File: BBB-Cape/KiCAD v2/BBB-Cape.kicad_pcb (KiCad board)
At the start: 2 copper layers, 54.6 x 86.4 mm, 85 parts, among them J1 MOUNTING_HOLE, J10 Conn_01x02, J11 RJ45-TRANSFO, J12 DB9_Female, J13 SPI1, J14 I2C2, J15 UART5, J16 5V PWR, J2 MOUNTING_HOLE, J3 MOUNTING_HOLE, J4 MOUNTING_HOLE, J9 01x06_Stackable Header, P8 02x23_Stackable Header, P9 02x23_Stackable Header, SW1 W5500_RST, SW2 SYS_RST, SW3 Power, U1 LM25576MH, U2 WIZnet W5500, U3 MAX13433EETD, Y1 25MHz

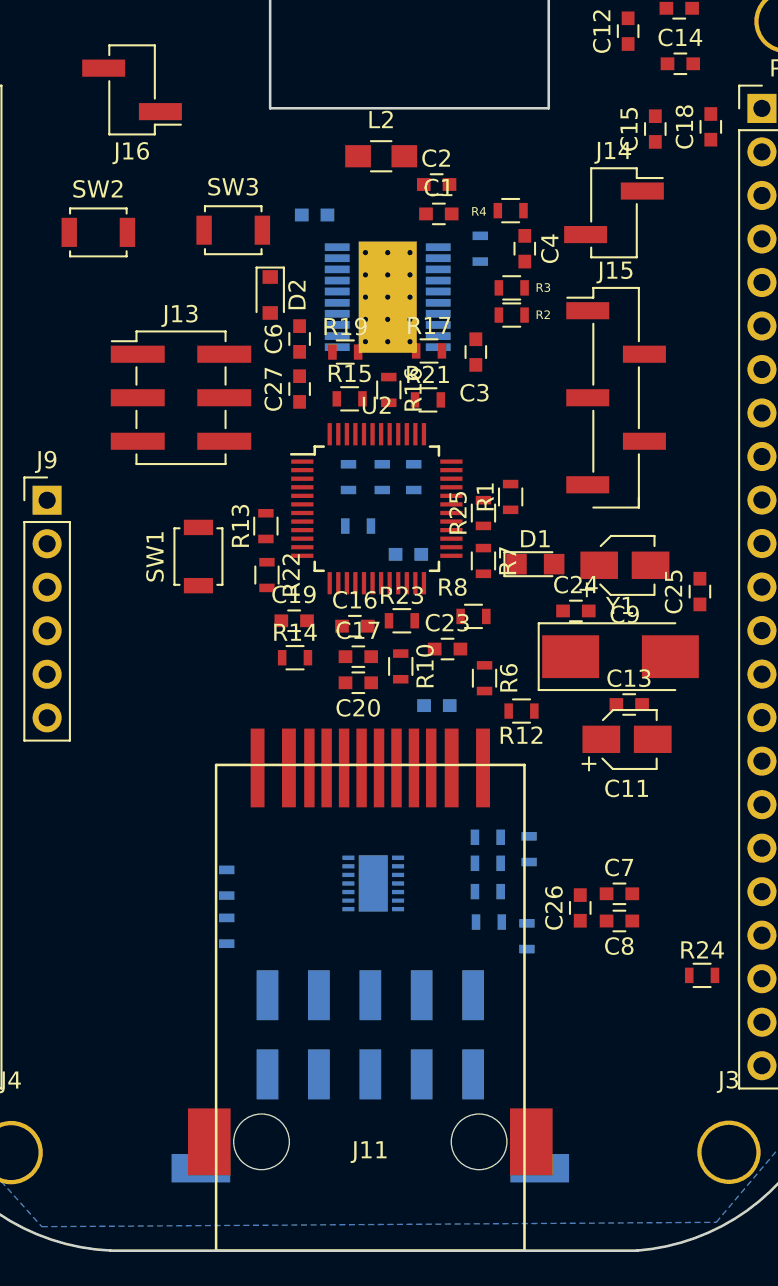
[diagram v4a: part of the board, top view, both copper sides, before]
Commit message: Connector Position Changes
Moved around the ethernet and RS485 connectors so they will not interfere with the BBB.
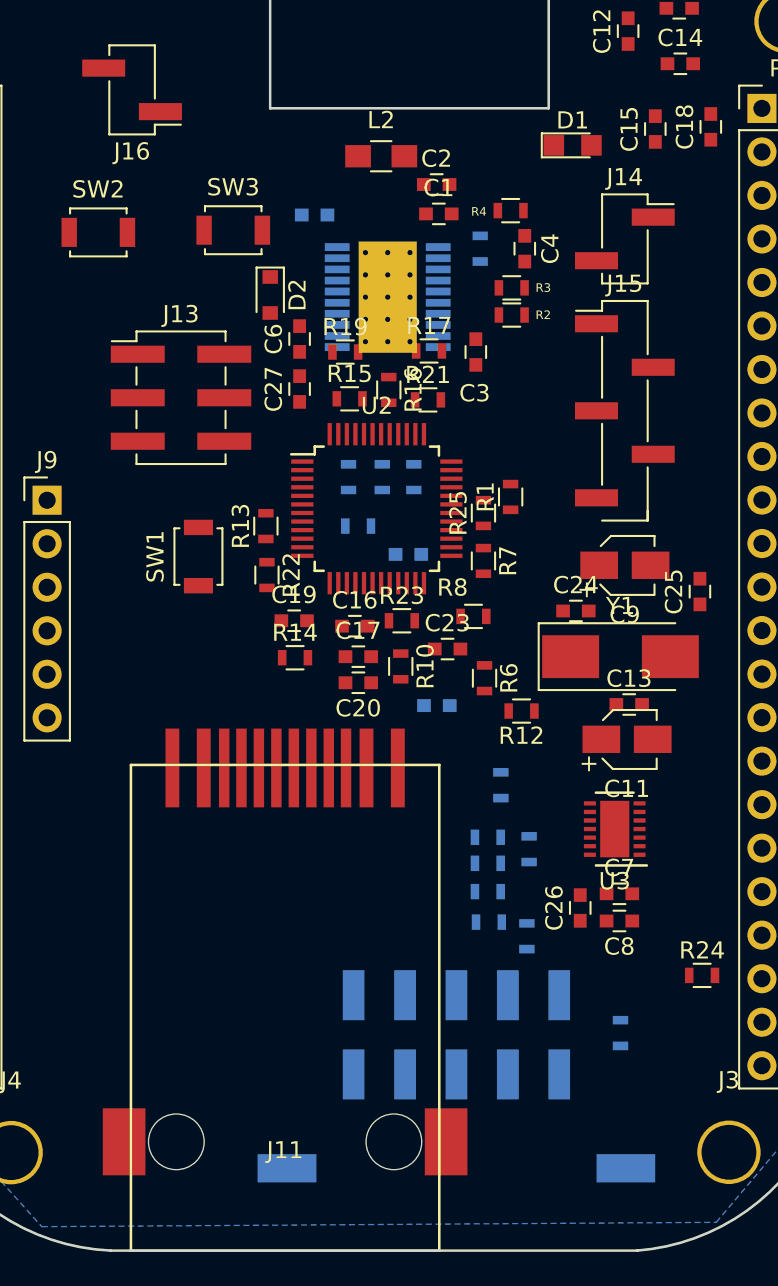
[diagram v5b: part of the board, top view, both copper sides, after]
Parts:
- U3: moved to F.Cu
- moved R32 24.6 mm to (152.6, 121.2)
- moved D1 24.5 mm to (149.8, 69.4)
- moved R33 18.1 mm to (145.6, 106.7)
- moved U3 14.5 mm to (152.2, 109.3)
- moved J12 5.03 mm to (143.0, 121.3)
- moved J11 4.97 mm to (133.0, 127.5)
- moved J14 1.65 mm to (152.8, 74.8)
- moved J15 0.92 mm to (152.8, 84.9)
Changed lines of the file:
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@@
   (general
     (links 206)
-    (no_connects 188)
-    (area 104.279275 45.8891 171.666326 168.8085)
+    (no_connects 187)
+    (area 110.592799 47.461099 165.352801 133.971101)
     (thickness 1.6)
     (drawings 12)
@@
   )
   (setup
-    (last_trace_width 0.254)
+    (last_trace_width 0.4064)
     (user_trace_width 0.254)
     (user_trace_width 0.3048)
@@
   )
   (module Connectors_Molex:Molex_MicroFit_3.0-43045-1010_10x3.00mm_Angled (layer B.Cu)
-    (at 137.9728 121.2991)
+    (at 143 121.2991)
     (descr "Molex Micro-Fit 3.0 connector, PN:43045-1010, top entry type, SMDhttp://www.molex.com/pdm_docs/sd/430450210_sd.pdf")
     (tags "conn molex micro fit 3.0")
@@
   )
   (module RJ45:RJ45_Surface_Mount (layer F.Cu)
-    (at 137.9728 127.5461)
+    (at 133 127.5461)
     (fp_text reference J11 (at 0 0.5) (layer F.SilkS)
       (effects (font (size 1 1) (thickness 0.15)))
@@
   )
   (module LEDs:LED_0805 (layer F.Cu)
-    (at 147.6043 93.8276)
+    (at 149.7838 69.3801)
     (descr "LED 0805 smd package")
     (tags "LED led 0805 SMD smd SMT smt smdled SMDLED smtled SMTLED")
@@
   )
   (module Resistors_SMD:R_0603 (layer B.Cu)
-    (at 129.5908 112.4211 90)
+    (at 152.5778 121.1961 90)
     (descr "Resistor SMD 0603, reflow soldering, Vishay (see dcrcw.pdf)")
     (tags "resistor 0603")
@@
   )
   (module Resistors_SMD:R_0603 (layer B.Cu)
-    (at 129.5908 115.2271 270)
+    (at 145.5928 106.7301 270)
     (descr "Resistor SMD 0603, reflow soldering, Vishay (see dcrcw.pdf)")
     (tags "resistor 0603")
@@
     )
   )
-  (module Housings_DFN_QFN:DFN-14-1EP_3x4mm_Pitch0.5mm (layer B.Cu)
-    (at 138.1438 112.4646 180)
+  (module Housings_DFN_QFN:DFN-14-1EP_3x4mm_Pitch0.5mm (layer F.Cu)
+    (at 152.2408 109.2896 180)
     (descr "DE Package; 14-Lead Plastic DFN (4mm x 3mm) (see Linear Technology DFN_14_05-08-1708.pdf)")
     (tags "DFN 0.5")
     (attr smd)
-    (fp_text reference U3 (at 0 3.05 180) (layer B.SilkS)
-      (effects (font (size 1 1) (thickness 0.15)) (justify mirror))
+    (fp_text reference U3 (at 0 -3.05 180) (layer F.SilkS)
+      (effects (font (size 1 1) (thickness 0.15)))
     )
-    (fp_text value MAX13433EETD (at 0 -3.05 180) (layer B.Fab)
-      (effects (font (size 1 1) (thickness 0.15)) (justify mirror))
+    (fp_text value MAX13433EETD (at 0 3.05 180) (layer F.Fab)
+      (effects (font (size 1 1) (thickness 0.15)))
     )
-    (fp_line (start -0.5 2) (end 1.5 2) (layer B.Fab) (width 0.15))
-    (fp_line (start 1.5 2) (end 1.5 -2) (layer B.Fab) (width 0.15))
-    (fp_line (start 1.5 -2) (end -1.5 -2) (layer B.Fab) (width 0.15))
-    (fp_line (start -1.5 -2) (end -1.5 1) (layer B.Fab) (width 0.15))
-    (fp_line (start -1.5 1) (end -0.5 2) (layer B.Fab) (width 0.15))
-    (fp_line (start -2.05 2.3) (end -2.05 -2.3) (layer B.CrtYd) (width 0.05))
-    (fp_line (start 2.05 2.3) (end 2.05 -2.3) (layer B.CrtYd) (width 0.05))
-    (fp_line (start -2.05 2.3) (end 2.05 2.3) (layer B.CrtYd) (width 0.05))
-    (fp_line (start -2.05 -2.3) (end 2.05 -2.3) (layer B.CrtYd) (width 0.05))
-    (fp_line (start -1.1 -2.125) (end 1.1 -2.125) (layer B.SilkS) (width 0.15))
-    (fp_line (start -1.875 2.125) (end 1.1 2.125) (layer B.SilkS) (width 0.15))
-    (pad 1 smd rect (at -1.45 1.5 180) (size 0.7 0.25) (layers B.Cu B.Paste B.Mask)
+    (fp_line (start -0.5 -2) (end 1.5 -2) (layer F.Fab) (width 0.15))
+    (fp_line (start 1.5 -2) (end 1.5 2) (layer F.Fab) (width 0.15))
+    (fp_line (start 1.5 2) (end -1.5 2) (layer F.Fab) (width 0.15))
+    (fp_line (start -1.5 2) (end -1.5 -1) (layer F.Fab) (width 0.15))
+    (fp_line (start -1.5 -1) (end -0.5 -2) (layer F.Fab) (width 0.15))
+    (fp_line (start -2.05 -2.3) (end -2.05 2.3) (layer F.CrtYd) (width 0.05))
+    (fp_line (start 2.05 -2.3) (end 2.05 2.3) (layer F.CrtYd) (width 0.05))
+    (fp_line (start -2.05 -2.3) (end 2.05 -2.3) (layer F.CrtYd) (width 0.05))
+    (fp_line (start -2.05 2.3) (end 2.05 2.3) (layer F.CrtYd) (width 0.05))
+    (fp_line (start -1.1 2.125) (end 1.1 2.125) (layer F.SilkS) (width 0.15))
+    (fp_line (start -1.875 -2.125) (end 1.1 -2.125) (layer F.SilkS) (width 0.15))
+    (pad 1 smd rect (at -1.45 -1.5 180) (size 0.7 0.25) (layers F.Cu F.Paste F.Mask)
       (net 9 VDD_5V))
-    (pad 2 smd rect (at -1.45 1 180) (size 0.7 0.25) (layers B.Cu B.Paste B.Mask)
+    (pad 2 smd rect (at -1.45 -1 180) (size 0.7 0.25) (layers F.Cu F.Paste F.Mask)
       (net 64 "Net-(R28-Pad1)"))
-    (pad 3 smd rect (at -1.45 0.5 180) (size 0.7 0.25) (layers B.Cu B.Paste B.Mask)
+    (pad 3 smd rect (at -1.45 -0.5 180) (size 0.7 0.25) (layers F.Cu F.Paste F.Mask)
       (net 67 "Net-(R31-Pad1)"))
-    (pad 4 smd rect (at -1.45 0 180) (size 0.7 0.25) (layers B.Cu B.Paste B.Mask)
+    (pad 4 smd rect (at -1.45 0 180) (size 0.7 0.25) (layers F.Cu F.Paste F.Mask)
       (net 65 "Net-(R29-Pad1)"))
-    (pad 5 smd rect (at -1.45 -0.5 180) (size 0.7 0.25) (layers B.Cu B.Paste B.Mask)
+    (pad 5 smd rect (at -1.45 0.5 180) (size 0.7 0.25) (layers F.Cu F.Paste F.Mask)
       (net 66 "Net-(R30-Pad1)"))
-    (pad 6 smd rect (at -1.45 -1 180) (size 0.7 0.25) (layers B.Cu B.Paste B.Mask)
+    (pad 6 smd rect (at -1.45 1 180) (size 0.7 0.25) (layers F.Cu F.Paste F.Mask)
       (net 3 DGND))
-    (pad 7 smd rect (at -1.45 -1.5 180) (size 0.7 0.25) (layers B.Cu B.Paste B.Mask)
+    (pad 7 smd rect (at -1.45 1.5 180) (size 0.7 0.25) (layers F.Cu F.Paste F.Mask)
       (net 153 "Net-(U3-Pad7)"))
-    (pad 8 smd rect (at 1.45 -1.5 180) (size 0.7 0.25) (layers B.Cu B.Paste B.Mask)
+    (pad 8 smd rect (at 1.45 1.5 180) (size 0.7 0.25) (layers F.Cu F.Paste F.Mask)
       (net 3 DGND))
-    (pad 9 smd rect (at 1.45 -1 180) (size 0.7 0.25) (layers B.Cu B.Paste B.Mask)
+    (pad 9 smd rect (at 1.45 1 180) (size 0.7 0.25) (layers F.Cu F.Paste F.Mask)
       (net 50 RS485_TX-))
-    (pad 10 smd rect (at 1.45 -0.5 180) (size 0.7 0.25) (layers B.Cu B.Paste B.Mask)
+    (pad 10 smd rect (at 1.45 0.5 180) (size 0.7 0.25) (layers F.Cu F.Paste F.Mask)
       (net 51 RS485_TX+))
-    (pad 11 smd rect (at 1.45 0 180) (size 0.7 0.25) (layers B.Cu B.Paste B.Mask)
+    (pad 11 smd rect (at 1.45 0 180) (size 0.7 0.25) (layers F.Cu F.Paste F.Mask)
       (net 52 RS485_RX+))
-    (pad 12 smd rect (at 1.45 0.5 180) (size 0.7 0.25) (layers B.Cu B.Paste B.Mask)
+    (pad 12 smd rect (at 1.45 -0.5 180) (size 0.7 0.25) (layers F.Cu F.Paste F.Mask)
       (net 53 RS485_RX-))
-    (pad 13 smd rect (at 1.45 1 180) (size 0.7 0.25) (layers B.Cu B.Paste B.Mask)
+    (pad 13 smd rect (at 1.45 -1 180) (size 0.7 0.25) (layers F.Cu F.Paste F.Mask)
       (net 154 "Net-(U3-Pad13)"))
-    (pad 14 smd rect (at 1.45 1.5 180) (size 0.7 0.25) (layers B.Cu B.Paste B.Mask)
+    (pad 14 smd rect (at 1.45 -1.5 180) (size 0.7 0.25) (layers F.Cu F.Paste F.Mask)
       (net 9 VDD_5V))
-    (pad 15 smd rect (at 0.425 -1.2375 180) (size 0.85 0.825) (layers B.Cu B.Paste B.Mask)
+    (pad 15 smd rect (at 0.425 1.2375 180) (size 0.85 0.825) (layers F.Cu F.Paste F.Mask)
       (net 3 DGND) (solder_paste_margin_ratio -0.2))
-    (pad 15 smd rect (at 0.425 -0.4125 180) (size 0.85 0.825) (layers B.Cu B.Paste B.Mask)
+    (pad 15 smd rect (at 0.425 0.4125 180) (size 0.85 0.825) (layers F.Cu F.Paste F.Mask)
       (net 3 DGND) (solder_paste_margin_ratio -0.2))
-    (pad 15 smd rect (at 0.425 0.4125 180) (size 0.85 0.825) (layers B.Cu B.Paste B.Mask)
+    (pad 15 smd rect (at 0.425 -0.4125 180) (size 0.85 0.825) (layers F.Cu F.Paste F.Mask)
       (net 3 DGND) (solder_paste_margin_ratio -0.2))
-    (pad 15 smd rect (at 0.425 1.2375 180) (size 0.85 0.825) (layers B.Cu B.Paste B.Mask)
+    (pad 15 smd rect (at 0.425 -1.2375 180) (size 0.85 0.825) (layers F.Cu F.Paste F.Mask)
       (net 3 DGND) (solder_paste_margin_ratio -0.2))
-    (pad 15 smd rect (at -0.425 -1.2375 180) (size 0.85 0.825) (layers B.Cu B.Paste B.Mask)
+    (pad 15 smd rect (at -0.425 1.2375 180) (size 0.85 0.825) (layers F.Cu F.Paste F.Mask)
       (net 3 DGND) (solder_paste_margin_ratio -0.2))
-    (pad 15 smd rect (at -0.425 -0.4125 180) (size 0.85 0.825) (layers B.Cu B.Paste B.Mask)
+    (pad 15 smd rect (at -0.425 0.4125 180) (size 0.85 0.825) (layers F.Cu F.Paste F.Mask)
       (net 3 DGND) (solder_paste_margin_ratio -0.2))
-    (pad 15 smd rect (at -0.425 0.4125 180) (size 0.85 0.825) (layers B.Cu B.Paste B.Mask)
+    (pad 15 smd rect (at -0.425 -0.4125 180) (size 0.85 0.825) (layers F.Cu F.Paste F.Mask)
       (net 3 DGND) (solder_paste_margin_ratio -0.2))
-    (pad 15 smd rect (at -0.425 1.2375 180) (size 0.85 0.825) (layers B.Cu B.Paste B.Mask)
+    (pad 15 smd rect (at -0.425 -1.2375 180) (size 0.85 0.825) (layers F.Cu F.Paste F.Mask)
       (net 3 DGND) (solder_paste_margin_ratio -0.2))
     (model ${KISYS3DMOD}/Housings_DFN_QFN.3dshapes/DFN-14-1EP_3x4mm_Pitch0.5mm.wrl
@@
   )
   (module Pin_Headers:Pin_Header_Straight_1x02_Pitch2.54mm_SMD_Pin1Right (layer F.Cu)
-    (at 152.1968 73.3171)
+    (at 152.8318 74.8411)
     (descr "surface-mounted straight pin header, 1x02, 2.54mm pitch, single row, style 2 (pin 1 right)")
     (tags "Surface mounted pin header SMD 1x02 2.54mm single row style2 pin1 right")
@@
   )
   (module Pin_Headers:Pin_Header_Straight_1x05_Pitch2.54mm_SMD_Pin1Left (layer F.Cu)
-    (at 152.3198 84.1121)
+    (at 152.8318 84.8741)
     (descr "surface-mounted straight pin header, 1x05, 2.54mm pitch, single row, style 1 (pin 1 left)")
     (tags "Surface mounted pin header SMD 1x05 2.54mm single row style1 pin1 left")
